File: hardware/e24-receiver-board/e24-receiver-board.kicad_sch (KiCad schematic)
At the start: 21 parts, among them J1 505070-2422, J10 SPEAKER-, J11 GND1, J12 TRACK_RIGHT, J13 MOTOR+, J14 LAMP_REAR, J15 CAP+, J16 U+, J17 AUX3, J18 AUX10, J19 AUX12, J2 TRACK_LEFT, J20 SPEAKER+, J21 GND2, J3 MOTOR-, J4 LAMP_FRONT, J5 VCC, J6 AUX1, J7 AUX2, J8 AUX4, J9 AUX11

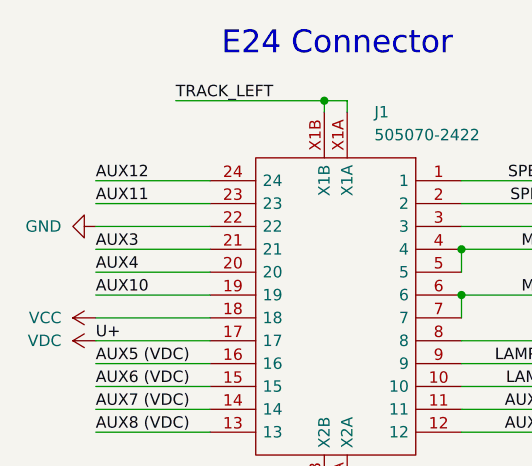
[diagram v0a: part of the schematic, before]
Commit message: fix: un-swap aux11/aux12 pins
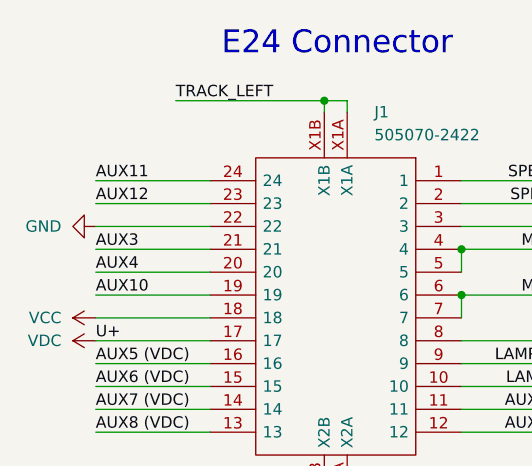
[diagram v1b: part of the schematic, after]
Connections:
- net AUX11: now also J1.24; no longer J1.23
- net AUX12: now also J1.23; no longer J1.24
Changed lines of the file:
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@@
 	)
 	(label "AUX12"
-		(at 49.53 39.37 0)
+		(at 49.53 41.91 0)
 		(effects
 			(font
@@
 	)
 	(label "AUX11"
-		(at 49.53 41.91 0)
-		(effects
-			(font
+		(at 49.53 39.37 0)
+		(effects
+			(font
